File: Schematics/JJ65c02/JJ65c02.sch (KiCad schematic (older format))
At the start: 22 parts, among them U1 74HC00, U2 74HC02, X1 1Mhz

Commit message: 6551 updates
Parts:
- removed A1: Arduino_Nano_v3.x, Module:Arduino_Nano, symbol MCU_Module:Arduino_Nano_v3.x
- added ACIA1: 65C51N, Package_DIP:DIP-28_W15.24mm_Socket, symbol 6502:65C51N
- added R?: 4.7K, symbol Device:R_US
- added U?: 74HC08, symbol 74xx:74LS08
- added X?: 1.8Mhz, Oscillator:Oscillator_DIP-14, symbol Oscillator:CXO_DIP14
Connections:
- net labels added: ACIA-CLK, AIRQ, IRQ, VIRQ
- wire segments 262 -> 284
- no-connect marks 14 -> 17
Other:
- note added: "Memory Map:\n$0000 - $7fff RAM: 32k\n $0000 - $00ff RAM: Zero Page\n $0100 - $01ff RAM: Stack pointer (sp) / Page 1\n$8000 - $8fff IO: 4K\n$9000 - $9fff VIA 1: 4K (a12 -> CS1)\n$a000 - $ffff ROM: 24K"
- note removed: "Memory Map:\n$0000 - $7fff RAM: 32k\n $0000 - $00ff RAM: Zero Page\n $0100 - $01ff RAM: Stack pointer (sp) / Page 1\n$8000 - $8fff VIA 2: 4K (not used) (a11 ->CS1)\n$9000 - $9fff VIA 1: 4K (a12 -> CS1)\n$a000 - $ffff ROM: 24K"
- moved on the sheet: X1

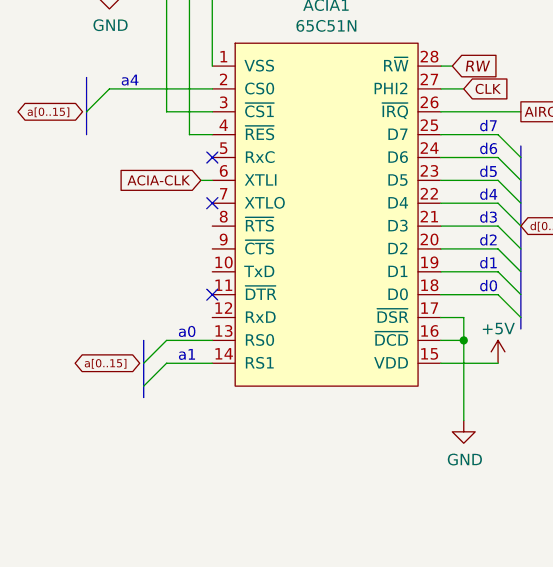
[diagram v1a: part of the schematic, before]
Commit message: Note wiring for ACIA chip re: h/w flow control
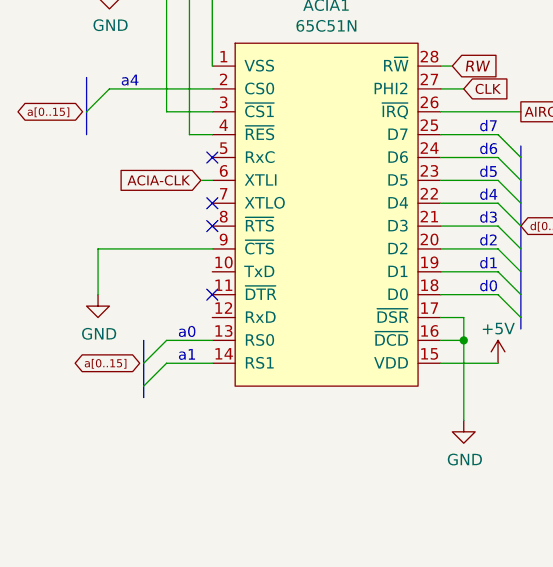
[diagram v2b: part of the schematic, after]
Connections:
- wire segments 284 -> 286
- no-connect marks 17 -> 18
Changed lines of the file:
@@
 NoConn ~ 1400 5550
 NoConn ~ 1400 5950
+NoConn ~ 1400 5650
+$Comp
+L power:GND #PWR?
+U 1 1 615AC011
+P 900 5950
+F 0 "#PWR?" H 900 5700 50  0001 C CNN
+F 1 "GND" H 905 5777 50  0000 C CNN
+F 2 "" H 900 5950 50  0001 C CNN
+F 3 "" H 900 5950 50  0001 C CNN
+	1    900  5950
+	1    0    0    -1
+$EndComp
+Wire Wire Line
+	1400 5750 900  5750
+Wire Wire Line
+	900  5750 900  5950
 Wire Bus Line
 	5150 3500 5150 3700

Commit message: Push updated schematics
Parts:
- removed C1: 0.1uF, symbol Device:C
- removed R1: 1K, symbol Device:R_Small_US
- removed R?: 4.7K, symbol Device:R_US
- removed Reset1: SW_Push, symbol Switch:SW_Push
- removed U1: 74HC00, symbol 74xx:74HC00
- removed U2: 74HC02, symbol 74xx:74HC02
- removed U?: 74HC08, symbol 74xx:74LS08
- removed X1: 1Mhz, Oscillator:Oscillator_DIP-14, symbol Oscillator:CXO_DIP14
- removed X?: 1.8Mhz, Oscillator:Oscillator_DIP-14, symbol Oscillator:CXO_DIP14
- added R10, R11: 1K, Resistor_THT:R_Axial_DIN0207_L6.3mm_D2.5mm_P7.62mm_Horizontal, symbol Device:R_Small_US
- added R2: 3.7K, Resistor_THT:R_Axial_DIN0207_L6.3mm_D2.5mm_P7.62mm_Horizontal, symbol Device:R_Small_US
- DB1, LB1, RB1, UB1: footprint (none) -> Button_Switch_THT:SW_PUSH_6mm_H4.3mm
- LEDDisplay1: footprint 16026-16X2 -> Display:WC1602A; symbol 6502:HD44780 -> Display_Character:NHD-0420H1Z
- R1: renamed from R2; footprint (none) -> Resistor_THT:R_Axial_DIN0207_L6.3mm_D2.5mm_P7.62mm_Horizontal
- R3, R4, R5, R6: footprint (none) -> Resistor_THT:R_Axial_DIN0207_L6.3mm_D2.5mm_P7.62mm_Horizontal
- RV1: footprint (none) -> Potentiometer_THT:Potentiometer_Bourns_3339P_Vertical
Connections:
- net labels added: IO~CS, RAM~CS, ROM~CE, ROM~OE, R~W, a0, a1, a10, a11, a12, a13, a14, a15, a2, a3, a4, a5, a6, a7, a8, a9, d0, d1, d2, d3, d4, d5, d6, d7, pb0, pb1, pb2, pb3, pb4, pb5, pb6, pb7, ~IRQ, ~RES
- net labels removed: AIRQ, IRQ, RW, VIRQ
- wire segments 286 -> 258
- no-connect marks 18 -> 16
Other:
- note added: "Main Schematic"
- note removed: "Memory Map:\n$0000 - $7fff RAM: 32k\n $0000 - $00ff RAM: Zero Page\n $0100 - $01ff RAM: Stack pointer (sp) / Page 1\n$8000 - $8fff IO: 4K\n$9000 - $9fff VIA 1: 4K (a12 -> CS1)\n$a000 - $ffff ROM: 24K"
- note removed: "a0"
- note removed: "a1"
- note removed: "a10"
- note removed: "a11"
- note removed: "a12"
- note removed: "a13"
- note removed: "a14"
- note removed: "a15"
- note removed: "a2"
- note removed: "a3"
- note removed: "a4"
- note removed: "a5"
- note removed: "a6"
- note removed: "a7"
- note removed: "a8"
- note removed: "a9"
- note removed: "d0"
- note removed: "d1"
- note removed: "d2"
- note removed: "d3"
- note removed: "d4"
- note removed: "d5"
- note removed: "d6"
- note removed: "d7"
- note removed: "pb0"
- note removed: "pb1"
- note removed: "pb2"
- note removed: "pb3"
- note removed: "pb4"
- note removed: "pb5"
- note removed: "pb6"
- note removed: "pb7"
- moved on the sheet: DB1, LB1, RAM1, RB1, ROM1, UB1

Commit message: Updates to reflect new memory map Use non-US symbols in Kicad
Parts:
- added R12: 3.3K, Resistor_THT:R_Axial_DIN0207_L6.3mm_D2.5mm_P7.62mm_Horizontal, symbol Device:R
- R1, R10, R11: value 1K -> 3.3K; symbol Device:R_Small_US -> Device:R
- R2, R3, R4, R5, R6: symbol Device:R_Small_US -> Device:R
- RV1: symbol Device:R_POT_TRIM_US -> Device:R_POT_TRIM
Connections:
- net +5V: now also R12.1; no longer CPU1.36 (BE)
- new net: CPU1.36 (BE), R12.2
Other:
- moved on the sheet: DB1, LB1, RB1, UB1
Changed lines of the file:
@@
 	3350 950  2900 950
 $Comp
-L Device:R_POT_TRIM_US RV1
+L Device:R_POT_TRIM RV1
 U 1 1 615573C8
 P 7050 5650
@@
 	850  900  850  1900
 $Comp
-L Device:R_Small_US R1
+L Device:R R1
 U 1 1 61ABC413
-P 1100 1900
-F 0 "R1" V 895 1900 50  0001 C CNN
-F 1 "1K" V 987 1900 50  0000 C CNN
-F 2 "Resistor_THT:R_Axial_DIN0207_L6.3mm_D2.5mm_P7.62mm_Horizontal" H 1100 1900 50  0001 C CNN
-F 3 "~" H 1100 1900 50  0001 C CNN
-	1    1100 1900
+P 1150 1900
+F 0 "R1" V 1050 1900 50  0000 C CNN
+F 1 "3.3K" V 1150 1900 50  0000 C CNN
+F 2 "Resistor_THT:R_Axial_DIN0207_L6.3mm_D2.5mm_P7.62mm_Horizontal" H 1150 1900 50  0001 C CNN
+F 3 "~" H 1150 1900 50  0001 C CNN
+	1    1150 1900
 	0    1    1    0
 $EndComp
-Wire Wire Line
-	1800 1900 1200 1900
 Wire Wire Line
 	4950 4250 4950 4800
@@
 	5100 5100 5100 4400
 NoConn ~ 4700 4700
-Wire Wire Line
-	2800 2200 3500 2200
 Wire Wire Line
 	3500 2200 3500 2050
@@
 L Switch:SW_Push UB1
 U 1 1 6136A5EF
-P 8400 5000
-F 0 "UB1" V 8300 5150 50  0000 C CNN
-F 1 "SW_Push" H 8400 5150 50  0001 C CNN
-F 2 "Button_Switch_THT:SW_PUSH_6mm_H4.3mm" H 8400 5200 50  0001 C CNN
-F 3 "~" H 8400 5200 50  0001 C CNN
-	1    8400 5000
+P 8400 4900
+F 0 "UB1" V 8300 5050 50  0000 C CNN
+F 1 "SW_Push" H 8400 5050 50  0001 C CNN
+F 2 "Button_Switch_THT:SW_PUSH_6mm_H4.3mm" H 8400 5100 50  0001 C CNN
+F 3 "~" H 8400 5100 50  0001 C CNN
+	1    8400 4900
 	0    1    1    0
 $EndComp
@@
 L Switch:SW_Push RB1
 U 1 1 61379F3D
-P 8700 5000
-F 0 "RB1" V 8600 5150 50  0000 C CNN
-F 1 "SW_Push" H 8700 5150 50  0001 C CNN
-F 2 "Button_Switch_THT:SW_PUSH_6mm_H4.3mm" H 8700 5200 50  0001 C CNN
-F 3 "~" H 8700 5200 50  0001 C CNN
-	1    8700 5000
+P 8700 4900
+F 0 "RB1" V 8600 5050 50  0000 C CNN
+F 1 "SW_Push" H 8700 5050 50  0001 C CNN
+F 2 "Button_Switch_THT:SW_PUSH_6mm_H4.3mm" H 8700 5100 50  0001 C CNN
+F 3 "~" H 8700 5100 50  0001 C CNN
+	1    8700 4900
 	0    1    1    0
 $EndComp
@@
 L Switch:SW_Push DB1
 U 1 1 6138977F
-P 9000 5000
-F 0 "DB1" V 8900 5150 50  0000 C CNN
-F 1 "SW_Push" H 9000 5150 50  0001 C CNN
-F 2 "Button_Switch_THT:SW_PUSH_6mm_H4.3mm" H 9000 5200 50  0001 C CNN
-F 3 "~" H 9000 5200 50  0001 C CNN
-	1    9000 5000
+P 9000 4900
+F 0 "DB1" V 8900 5050 50  0000 C CNN
+F 1 "SW_Push" H 9000 5050 50  0001 C CNN
+F 2 "Button_Switch_THT:SW_PUSH_6mm_H4.3mm" H 9000 5100 50  0001 C CNN
+F 3 "~" H 9000 5100 50  0001 C CNN
+	1    9000 4900
 	0    1    1    0
 $EndComp
 $Comp
-L Device:R_Small_US R6
+L Device:R R6
 U 1 1 613C0CBF
-P 9000 5300
-F 0 "R6" V 8795 5300 50  0001 C CNN
-F 1 "1K" V 8887 5300 50  0000 C CNN
-F 2 "Resistor_THT:R_Axial_DIN0207_L6.3mm_D2.5mm_P7.62mm_Horizontal" H 9000 5300 50  0001 C CNN
-F 3 "~" H 9000 5300 50  0001 C CNN
-	1    9000 5300
+P 9000 5250
+F 0 "R6" H 8900 5100 50  0000 C CNN
+F 1 "1K" V 9000 5250 50  0000 C CNN
+F 2 "Resistor_THT:R_Axial_DIN0207_L6.3mm_D2.5mm_P7.62mm_Horizontal" H 9000 5250 50  0001 C CNN
+F 3 "~" H 9000 5250 50  0001 C CNN
+	1    9000 5250
 	-1   0    0    1
 $EndComp
 $Comp
-L Device:R_Small_US R5
+L Device:R R5
 U 1 1 613C09A0
-P 8700 5300
-F 0 "R5" V 8495 5300 50  0001 C CNN
-F 1 "1K" V 8587 5300 50  0000 C CNN
-F 2 "Resistor_THT:R_Axial_DIN0207_L6.3mm_D2.5mm_P7.62mm_Horizontal" H 8700 5300 50  0001 C CNN
-F 3 "~" H 8700 5300 50  0001 C CNN
-	1    8700 5300
+P 8700 5250
+F 0 "R5" H 8600 5100 50  0000 C CNN
+F 1 "1K" V 8700 5250 50  0000 C CNN
+F 2 "Resistor_THT:R_Axial_DIN0207_L6.3mm_D2.5mm_P7.62mm_Horizontal" H 8700 5250 50  0001 C CNN
+F 3 "~" H 8700 5250 50  0001 C CNN
+	1    8700 5250
 	-1   0    0    1
 $EndComp
 $Comp
-L Device:R_Small_US R4
+L Device:R R4
 U 1 1 613C0477
-P 8400 5300
-F 0 "R4" V 8195 5300 50  0001 C CNN
-F 1 "1K" V 8287 5300 50  0000 C CNN
-F 2 "Resistor_THT:R_Axial_DIN0207_L6.3mm_D2.5mm_P7.62mm_Horizontal" H 8400 5300 50  0001 C CNN
-F 3 "~" H 8400 5300 50  0001 C CNN
-	1    8400 5300
+P 8400 5250
+F 0 "R4" H 8300 5100 50  0000 C CNN
+F 1 "1K" V 8400 5250 50  0000 C CNN
+F 2 "Resistor_THT:R_Axial_DIN0207_L6.3mm_D2.5mm_P7.62mm_Horizontal" H 8400 5250 50  0001 C CNN
+F 3 "~" H 8400 5250 50  0001 C CNN
+	1    8400 5250
 	-1   0    0    1
 $EndComp
 $Comp
-L Device:R_Small_US R3
+L Device:R R3
 U 1 1 613AF256
-P 8100 5300
-F 0 "R3" V 7895 5300 50  0001 C CNN
-F 1 "1K" V 7987 5300 50  0000 C CNN
-F 2 "Resistor_THT:R_Axial_DIN0207_L6.3mm_D2.5mm_P7.62mm_Horizontal" H 8100 5300 50  0001 C CNN
-F 3 "~" H 8100 5300 50  0001 C CNN
-	1    8100 5300
+P 8100 5250
+F 0 "R3" H 8000 5100 50  0000 C CNN
+F 1 "1K" V 8100 5250 50  0000 C CNN
+F 2 "Resistor_THT:R_Axial_DIN0207_L6.3mm_D2.5mm_P7.62mm_Horizontal" H 8100 5250 50  0001 C CNN
+F 3 "~" H 8100 5250 50  0001 C CNN
+	1    8100 5250
 	-1   0    0    1
 $EndComp
@@
 L power:+5V #PWR013
 U 1 1 614170CA
-P 8550 4700
-F 0 "#PWR013" H 8550 4550 50  0001 C CNN
-F 1 "+5V" H 8565 4873 50  0000 C CNN
-F 2 "" H 8550 4700 50  0001 C CNN
-F 3 "" H 8550 4700 50  0001 C CNN
-	1    8550 4700
-	1    0    0    -1
-$EndComp
-Wire Wire Line
-	9000 4800 8700 4800
-Connection ~ 8400 4800
-Wire Wire Line
-	8400 4800 8100 4800
-Connection ~ 8700 4800
-Wire Wire Line
-	8700 4800 8550 4800
-Wire Wire Line
-	8550 4700 8550 4800
-Connection ~ 8550 4800
-Wire Wire Line
-	8550 4800 8400 4800
+P 8550 4600
+F 0 "#PWR013" H 8550 4450 50  0001 C CNN
+F 1 "+5V" H 8565 4773 50  0000 C CNN
+F 2 "" H 8550 4600 50  0001 C CNN
+F 3 "" H 8550 4600 50  0001 C CNN
+	1    8550 4600
+	1    0    0    -1
+$EndComp
+Wire Wire Line
+	9000 4700 8700 4700
+Connection ~ 8400 4700
+Wire Wire Line
+	8400 4700 8100 4700
+Connection ~ 8700 4700
+Wire Wire Line
+	8700 4700 8550 4700
+Wire Wire Line
+	8550 4600 8550 4700
+Connection ~ 8550 4700
+Wire Wire Line
+	8550 4700 8400 4700
 Wire Wire Line
 	8700 5400 8700 5650
@@
 L Switch:SW_Push LB1
 U 1 1 613599F4
-P 8100 5000
-F 0 "LB1" V 8000 5150 50  0000 C CNN
-F 1 "SW_Push" H 8100 5150 50  0001 C CNN
-F 2 "Button_Switch_THT:SW_PUSH_6mm_H4.3mm" H 8100 5200 50  0001 C CNN
-F 3 "~" H 8100 5200 50  0001 C CNN
-	1    8100 5000
+P 8100 4900
+F 0 "LB1" V 8000 5050 50  0000 C CNN
+F 1 "SW_Push" H 8100 5050 50  0001 C CNN
+F 2 "Button_Switch_THT:SW_PUSH_6mm_H4.3mm" H 8100 5100 50  0001 C CNN
+F 3 "~" H 8100 5100 50  0001 C CNN
+	1    8100 4900
 	0    1    1    0
 $EndComp
@@
 Text GLabel 1050 2700 0    43   Input ~ 0
 ~IRQ
-Wire Wire Line
-	1800 2300 1200 2300
 Wire Wire Line
 	850  2300 850  2100
@@
 ROM~OE
 $Comp
-L Device:R_Small_US R2
+L Device:R R2
 U 1 1 615CB631
-P 1100 2100
-F 0 "R2" V 895 2100 50  0001 C CNN
-F 1 "3.7K" V 987 2100 50  0000 C CNN
-F 2 "Resistor_THT:R_Axial_DIN0207_L6.3mm_D2.5mm_P7.62mm_Horizontal" H 1100 2100 50  0001 C CNN
-F 3 "~" H 1100 2100 50  0001 C CNN
-	1    1100 2100
+P 1150 2100
+F 0 "R2" V 1050 2100 50  0000 C CNN
+F 1 "3.7K" V 1150 2100 50  0000 C CNN
+F 2 "Resistor_THT:R_Axial_DIN0207_L6.3mm_D2.5mm_P7.62mm_Horizontal" H 1150 2100 50  0001 C CNN
+F 3 "~" H 1150 2100 50  0001 C CNN
+	1    1150 2100
 	0    1    1    0
 $EndComp
@@
 Wire Wire Line
 	850  2100 850  1900
-Wire Wire Line
-	1200 2100 1300 2100
-Wire Wire Line
-	1050 2700 1300 2700
-Wire Wire Line
-	1300 2700 1300 2100
-Connection ~ 1300 2100
-Wire Wire Line
-	1300 2100 1800 2100
 Wire Wire Line
 	6800 1400 6800 2550
@@
 Connection ~ 4850 6750
 $Comp
-L Device:R_Small_US R10
+L Device:R R10
 U 1 1 615E6635
-P 1100 2300
-F 0 "R10" V 895 2300 50  0001 C CNN
-F 1 "1K" V 987 2300 50  0000 C CNN
-F 2 "Resistor_THT:R_Axial_DIN0207_L6.3mm_D2.5mm_P7.62mm_Horizontal" H 1100 2300 50  0001 C CNN
-F 3 "~" H 1100 2300 50  0001 C CNN
-	1    1100 2300
+P 1150 2300
+F 0 "R10" V 1050 2300 50  0000 C CNN
+F 1 "3.3K" V 1150 2300 50  0000 C CNN
+F 2 "Resistor_THT:R_Axial_DIN0207_L6.3mm_D2.5mm_P7.62mm_Horizontal" H 1150 2300 50  0001 C CNN
+F 3 "~" H 1150 2300 50  0001 C CNN
+	1    1150 2300
 	0    1    1    0
 $EndComp
@@
 	8800 1800 8800 1950
 $Comp
-L Device:R_Small_US R11
+L Device:R R11
 U 1 1 616329C6
-P 9100 1950
-F 0 "R11" V 8895 1950 50  0001 C CNN
-F 1 "1K" V 8987 1950 50  0000 C CNN
-F 2 "Resistor_THT:R_Axial_DIN0207_L6.3mm_D2.5mm_P7.62mm_Horizontal" H 9100 1950 50  0001 C CNN
-F 3 "~" H 9100 1950 50  0001 C CNN
-	1    9100 1950
+P 9150 1950
+F 0 "R11" V 9050 1950 50  0000 C CNN
+F 1 "3.3K" V 9150 1950 50  0000 C CNN
+F 2 "Resistor_THT:R_Axial_DIN0207_L6.3mm_D2.5mm_P7.62mm_Horizontal" H 9150 1950 50  0001 C CNN
+F 3 "~" H 9150 1950 50  0001 C CNN
+	1    9150 1950
 	0    1    1    0
 $EndComp
 Wire Wire Line
 	8800 1800 9350 1800
-Wire Wire Line
-	9200 1950 9350 1950
-Wire Wire Line
-	9350 1950 9350 1800
-Connection ~ 9350 1800
 Wire Wire Line
 	9000 1950 8900 1950
@@
 $EndComp
 $Comp
-L power:GND #PWR?
+L power:GND #PWR0106
 U 1 1 615D7846
 P 6300 6400
-F 0 "#PWR?" H 6300 6150 50  0001 C CNN
+F 0 "#PWR0106" H 6300 6150 50  0001 C CNN
 F 1 "GND" H 6305 6227 50  0000 C CNN
 F 2 "" H 6300 6400 50  0001 C CNN
@@
 	6700 6400 6800 6400
 $Comp
-L power:+5V #PWR?
+L power:+5V #PWR0107
 U 1 1 6168F0BD
 P 6800 6400
-F 0 "#PWR?" H 6800 6250 50  0001 C CNN
+F 0 "#PWR0107" H 6800 6250 50  0001 C CNN
 F 1 "+5V" H 6800 6550 50  0000 C CNN
 F 2 "" H 6800 6400 50  0001 C CNN
@@
 Wire Wire Line
 	5100 4400 7850 4400
+$Comp
+L Device:R R12
+U 1 1 615D9CDA
+P 3150 2200
+F 0 "R12" V 3050 2200 50  0000 C CNN
+F 1 "3.3K" V 3150 2200 50  0000 C CNN
+F 2 "Resistor_THT:R_Axial_DIN0207_L6.3mm_D2.5mm_P7.62mm_Horizontal" H 3150 2200 50  0001 C CNN
+F 3 "~" H 3150 2200 50  0001 C CNN
+	1    3150 2200
+	0    1    1    0
+$EndComp
+Wire Wire Line
+	3300 2200 3500 2200
+Wire Wire Line
+	3000 2200 2800 2200
+Wire Wire Line
+	9300 1950 9350 1950
+Wire Wire Line
+	9350 1950 9350 1800
+Connection ~ 9350 1800
+Wire Wire Line
+	1300 1900 1800 1900
+Wire Wire Line
+	1800 2100 1400 2100
+Wire Wire Line
+	1300 2300 1800 2300
+Wire Wire Line
+	1400 2700 1400 2100
+Wire Wire Line
+	1050 2700 1400 2700
 Wire Bus Line
 	5150 3050 5150 3250
@@
 Wire Bus Line
 	1550 2700 1550 4100
+Connection ~ 1400 2100
+Wire Wire Line
+	1400 2100 1300 2100
 $EndSCHEMATC
